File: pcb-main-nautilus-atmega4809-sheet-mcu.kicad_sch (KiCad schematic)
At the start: 20 parts, among them SW1 PTS645SH43SMTR92 LFS, U4 ATmega4809-A

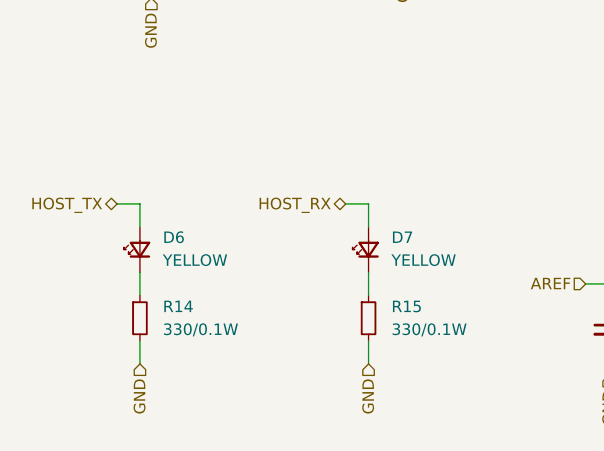
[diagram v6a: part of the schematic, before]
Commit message: Fix serial activity LEDs wiring
Supports #2.
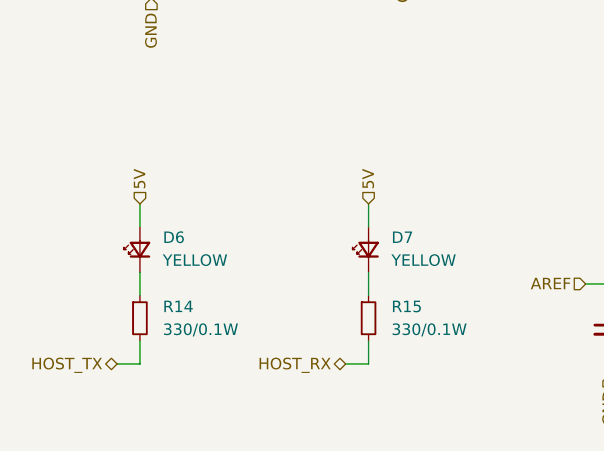
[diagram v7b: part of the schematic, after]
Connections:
- net 5V: now also D6.2 (A), D7.2 (A)
- net GND: no longer R14.2, R15.2
- net HOST_RX: now also R15.2; no longer D7.2 (A)
- net HOST_TX: now also R14.2; no longer D6.2 (A)
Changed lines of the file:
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@@
+    (stroke (width 0) (type default) (color 0 0 0 0))
+  )
+  (wire (pts (xy 44.45 127) (xy 44.45 129.54))
     (stroke (width 0) (type default) (color 0 0 0 0))
   )
@@
     (stroke (width 0) (type default) (color 0 0 0 0))
   )
+  (wire (pts (xy 142.24 54.61) (xy 142.24 64.77))
+    (stroke (width 0) (type default) (color 0 0 0 0))
+  )
+  (wire (pts (xy 147.32 64.77) (xy 142.24 64.77))
+    (stroke (width 0) (type default) (color 0 0 0 0))
+  )
+  (wire (pts (xy 67.31 144.78) (xy 69.85 144.78))
+    (stroke (width 0) (type default) (color 0 0 0 0))
+  )
+  (wire (pts (xy 154.94 102.87) (xy 157.48 102.87))
+    (stroke (width 0) (type default) (color 0 0 0 0))
+  )
+  (wire (pts (xy 73.66 96.52) (xy 73.66 99.06))
+    (stroke (width 0) (type default) (color 0 0 0 0))
+  )
+  (wire (pts (xy 154.94 133.35) (xy 157.48 133.35))
+    (stroke (width 0) (type default) (color 0 0 0 0))
+  )
+  (wire (pts (xy 71.12 88.9) (xy 73.66 88.9))
+    (stroke (width 0) (type default) (color 0 0 0 0))
+  )
+  (wire (pts (xy 198.12 78.74) (xy 200.66 78.74))
+    (stroke (width 0) (type default) (color 0 0 0 0))
+  )
+  (wire (pts (xy 121.92 87.63) (xy 124.46 87.63))
+    (stroke (width 0) (type default) (color 0 0 0 0))
+  )
+  (wire (pts (xy 73.66 88.9) (xy 73.66 91.44))
+    (stroke (width 0) (type default) (color 0 0 0 0))
+  )
+  (wire (pts (xy 198.12 76.2) (xy 200.66 76.2))
+    (stroke (width 0) (type default) (color 0 0 0 0))
+  )
+  (wire (pts (xy 111.76 135.89) (xy 111.76 138.43))
+    (stroke (width 0) (type default) (color 0 0 0 0))
+  )
+  (wire (pts (xy 121.92 92.71) (xy 124.46 92.71))
+    (stroke (width 0) (type default) (color 0 0 0 0))
+  )
+  (wire (pts (xy 205.74 76.2) (xy 208.28 76.2))
+    (stroke (width 0) (type default) (color 0 0 0 0))
+  )
+  (wire (pts (xy 205.74 88.9) (xy 208.28 88.9))
+    (stroke (width 0) (type default) (color 0 0 0 0))
+  )
+  (wire (pts (xy 147.32 54.61) (xy 142.24 54.61))
+    (stroke (width 0) (type default) (color 0 0 0 0))
+  )
+  (wire (pts (xy 154.94 128.27) (xy 157.48 128.27))
+    (stroke (width 0) (type default) (color 0 0 0 0))
+  )
+  (wire (pts (xy 154.94 100.33) (xy 157.48 100.33))
+    (stroke (width 0) (type default) (color 0 0 0 0))
+  )
+  (wire (pts (xy 198.12 88.9) (xy 200.66 88.9))
+    (stroke (width 0) (type default) (color 0 0 0 0))
+  )
+  (wire (pts (xy 124.46 44.45) (xy 124.46 54.61))
+    (stroke (width 0) (type default) (color 0 0 0 0))
+  )
+  (wire (pts (xy 45.72 101.6) (xy 45.72 104.14))
+    (stroke (width 0) (type default) (color 0 0 0 0))
+  )
+  (wire (pts (xy 139.7 64.77) (xy 139.7 72.39))
+    (stroke (width 0) (type default) (color 0 0 0 0))
+  )
+  (wire (pts (xy 121.92 107.95) (xy 124.46 107.95))
+    (stroke (width 0) (type default) (color 0 0 0 0))
+  )
+  (wire (pts (xy 96.52 138.43) (xy 96.52 135.89))
+    (stroke (width 0) (type default) (color 0 0 0 0))
+  )
+  (wire (pts (xy 124.46 54.61) (xy 124.46 64.77))
+    (stroke (width 0) (type default) (color 0 0 0 0))
+  )
+  (wire (pts (xy 129.54 44.45) (xy 124.46 44.45))
+    (stroke (width 0) (type default) (color 0 0 0 0))
+  )
   (wire (pts (xy 44.45 142.24) (xy 44.45 144.78))
     (stroke (width 0) (type default) (color 0 0 0 0))
   )
-  (wire (pts (xy 142.24 54.61) (xy 142.24 64.77))
-    (stroke (width 0) (type default) (color 0 0 0 0))
-  )
-  (wire (pts (xy 147.32 64.77) (xy 142.24 64.77))
-    (stroke (width 0) (type default) (color 0 0 0 0))
-  )
-  (wire (pts (xy 154.94 102.87) (xy 157.48 102.87))
-    (stroke (width 0) (type default) (color 0 0 0 0))
-  )
-  (wire (pts (xy 73.66 96.52) (xy 73.66 99.06))
-    (stroke (width 0) (type default) (color 0 0 0 0))
-  )
-  (wire (pts (xy 154.94 133.35) (xy 157.48 133.35))
-    (stroke (width 0) (type default) (color 0 0 0 0))
-  )
-  (wire (pts (xy 71.12 88.9) (xy 73.66 88.9))
-    (stroke (width 0) (type default) (color 0 0 0 0))
-  )
-  (wire (pts (xy 198.12 78.74) (xy 200.66 78.74))
-    (stroke (width 0) (type default) (color 0 0 0 0))
-  )
-  (wire (pts (xy 121.92 87.63) (xy 124.46 87.63))
-    (stroke (width 0) (type default) (color 0 0 0 0))
-  )
-  (wire (pts (xy 73.66 88.9) (xy 73.66 91.44))
-    (stroke (width 0) (type default) (color 0 0 0 0))
-  )
-  (wire (pts (xy 198.12 76.2) (xy 200.66 76.2))
-    (stroke (width 0) (type default) (color 0 0 0 0))
-  )
-  (wire (pts (xy 111.76 135.89) (xy 111.76 138.43))
-    (stroke (width 0) (type default) (color 0 0 0 0))
-  )
-  (wire (pts (xy 121.92 92.71) (xy 124.46 92.71))
-    (stroke (width 0) (type default) (color 0 0 0 0))
-  )
-  (wire (pts (xy 205.74 76.2) (xy 208.28 76.2))
-    (stroke (width 0) (type default) (color 0 0 0 0))
-  )
-  (wire (pts (xy 205.74 88.9) (xy 208.28 88.9))
-    (stroke (width 0) (type default) (color 0 0 0 0))
-  )
-  (wire (pts (xy 147.32 54.61) (xy 142.24 54.61))
-    (stroke (width 0) (type default) (color 0 0 0 0))
-  )
-  (wire (pts (xy 154.94 128.27) (xy 157.48 128.27))
-    (stroke (width 0) (type default) (color 0 0 0 0))
-  )
-  (wire (pts (xy 154.94 100.33) (xy 157.48 100.33))
-    (stroke (width 0) (type default) (color 0 0 0 0))
-  )
-  (wire (pts (xy 198.12 88.9) (xy 200.66 88.9))
-    (stroke (width 0) (type default) (color 0 0 0 0))
-  )
-  (wire (pts (xy 124.46 44.45) (xy 124.46 54.61))
-    (stroke (width 0) (type default) (color 0 0 0 0))
-  )
-  (wire (pts (xy 45.72 101.6) (xy 45.72 104.14))
-    (stroke (width 0) (type default) (color 0 0 0 0))
-  )
-  (wire (pts (xy 139.7 64.77) (xy 139.7 72.39))
-    (stroke (width 0) (type default) (color 0 0 0 0))
-  )
-  (wire (pts (xy 121.92 107.95) (xy 124.46 107.95))
-    (stroke (width 0) (type default) (color 0 0 0 0))
-  )
-  (wire (pts (xy 96.52 138.43) (xy 96.52 135.89))
-    (stroke (width 0) (type default) (color 0 0 0 0))
-  )
-  (wire (pts (xy 124.46 54.61) (xy 124.46 64.77))
-    (stroke (width 0) (type default) (color 0 0 0 0))
-  )
-  (wire (pts (xy 129.54 44.45) (xy 124.46 44.45))
-    (stroke (width 0) (type default) (color 0 0 0 0))
-  )
-  (wire (pts (xy 41.91 127) (xy 44.45 127))
-    (stroke (width 0) (type default) (color 0 0 0 0))
-  )
   (wire (pts (xy 121.92 105.41) (xy 124.46 105.41))
     (stroke (width 0) (type default) (color 0 0 0 0))
@@
     (stroke (width 0) (type default) (color 0 0 0 0))
   )
+  (wire (pts (xy 69.85 144.78) (xy 69.85 142.24))
+    (stroke (width 0) (type default) (color 0 0 0 0))
+  )
   (wire (pts (xy 69.85 134.62) (xy 69.85 137.16))
     (stroke (width 0) (type default) (color 0 0 0 0))
@@
     (stroke (width 0) (type default) (color 0 0 0 0))
   )
-  (wire (pts (xy 44.45 127) (xy 44.45 129.54))
-    (stroke (width 0) (type default) (color 0 0 0 0))
-  )
   (wire (pts (xy 124.46 54.61) (xy 129.54 54.61))
     (stroke (width 0) (type default) (color 0 0 0 0))
@@
     (stroke (width 0) (type default) (color 0 0 0 0))
   )
-  (wire (pts (xy 67.31 127) (xy 69.85 127))
-    (stroke (width 0) (type default) (color 0 0 0 0))
-  )
   (wire (pts (xy 154.94 130.81) (xy 157.48 130.81))
     (stroke (width 0) (type default) (color 0 0 0 0))
@@
     (stroke (width 0) (type default) (color 0 0 0 0))
   )
-  (wire (pts (xy 69.85 142.24) (xy 69.85 144.78))
-    (stroke (width 0) (type default) (color 0 0 0 0))
-  )
   (wire (pts (xy 96.52 143.51) (xy 96.52 146.05))
     (stroke (width 0) (type default) (color 0 0 0 0))
   )
+  (wire (pts (xy 44.45 144.78) (xy 41.91 144.78))
+    (stroke (width 0) (type default) (color 0 0 0 0))
+  )
   (wire (pts (xy 154.94 82.55) (xy 157.48 82.55))
     (stroke (width 0) (type default) (color 0 0 0 0))
@@
     (stroke (width 0) (type default) (color 0 0 0 0))
   )
+  (wire (pts (xy 69.85 127) (xy 69.85 129.54))
+    (stroke (width 0) (type default) (color 0 0 0 0))
+  )
   (wire (pts (xy 157.48 54.61) (xy 157.48 64.77))
     (stroke (width 0) (type default) (color 0 0 0 0))
@@
   )
   (wire (pts (xy 139.7 143.51) (xy 139.7 146.05))
-    (stroke (width 0) (type default) (color 0 0 0 0))
-  )
-  (wire (pts (xy 69.85 127) (xy 69.85 129.54))
     (stroke (width 0) (type default) (color 0 0 0 0))
   )
@@
     (effects (font (size 1.27 1.27)) (justify left))
   )
-  (hierarchical_label "HOST_TX" (shape bidirectional) (at 41.91 127 180)
-    (effects (font (size 1.27 1.27)) (justify right))
-  )
-  (hierarchical_label "GND" (shape input) (at 44.45 144.78 270)
+  (hierarchical_label "HOST_TX" (shape bidirectional) (at 41.91 144.78 180)
     (effects (font (size 1.27 1.27)) (justify right))
   )
@@
     (effects (font (size 1.27 1.27)) (justify right))
   )
-  (hierarchical_label "HOST_RX" (shape bidirectional) (at 67.31 127 180)
+  (hierarchical_label "HOST_RX" (shape bidirectional) (at 67.31 144.78 180)
     (effects (font (size 1.27 1.27)) (justify right))
   )
@@
     (effects (font (size 1.27 1.27)) (justify right))
   )
+  (hierarchical_label "5V" (shape input) (at 69.85 127 90)
+    (effects (font (size 1.27 1.27)) (justify left))
+  )
   (hierarchical_label "UPDI" (shape bidirectional) (at 121.92 77.47 180)
     (effects (font (size 1.27 1.27)) (justify right))
@@
     (effects (font (size 1.27 1.27)) (justify right))
   )
-  (hierarchical_label "GND" (shape input) (at 69.85 144.78 270)
-    (effects (font (size 1.27 1.27)) (justify right))
-  )
   (hierarchical_label "~{RESET}" (shape bidirectional) (at 76.2 88.9 0)
     (effects (font (size 1.27 1.27)) (justify left))
@@
     (effects (font (size 1.27 1.27)) (justify right))
   )
+  (hierarchical_label "5V" (shape input) (at 44.45 127 90)
+    (effects (font (size 1.27 1.27)) (justify left))
+  )
   (symbol (lib_id "Device:R_Small") (at 203.2 114.3 0) (unit 1)

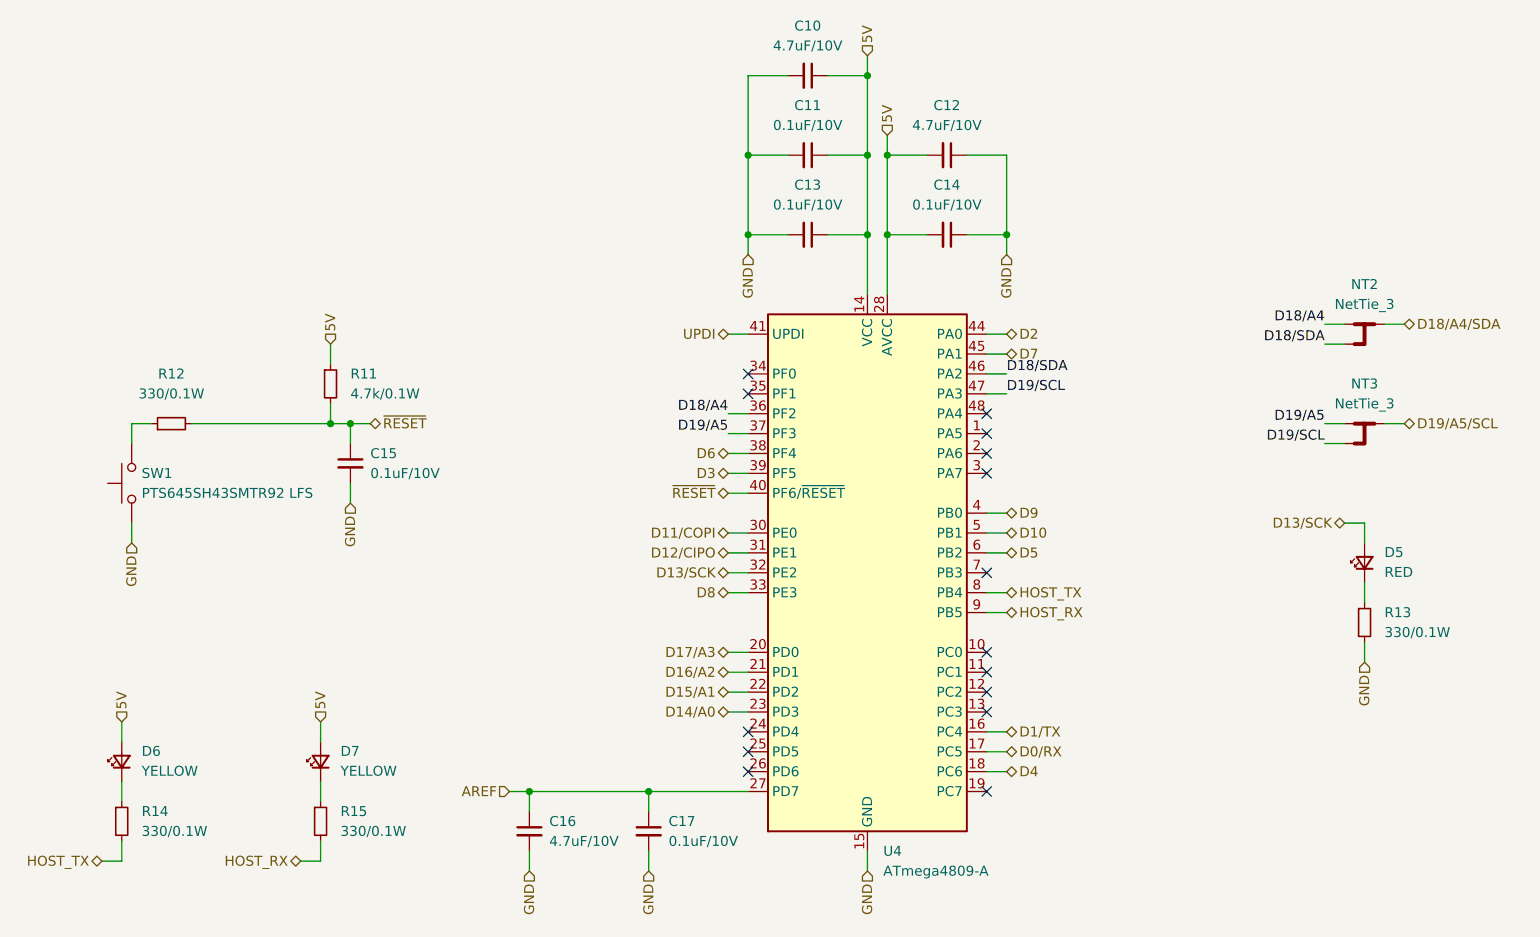
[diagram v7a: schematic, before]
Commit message: Improve MCU sheet flow
Supports #2.
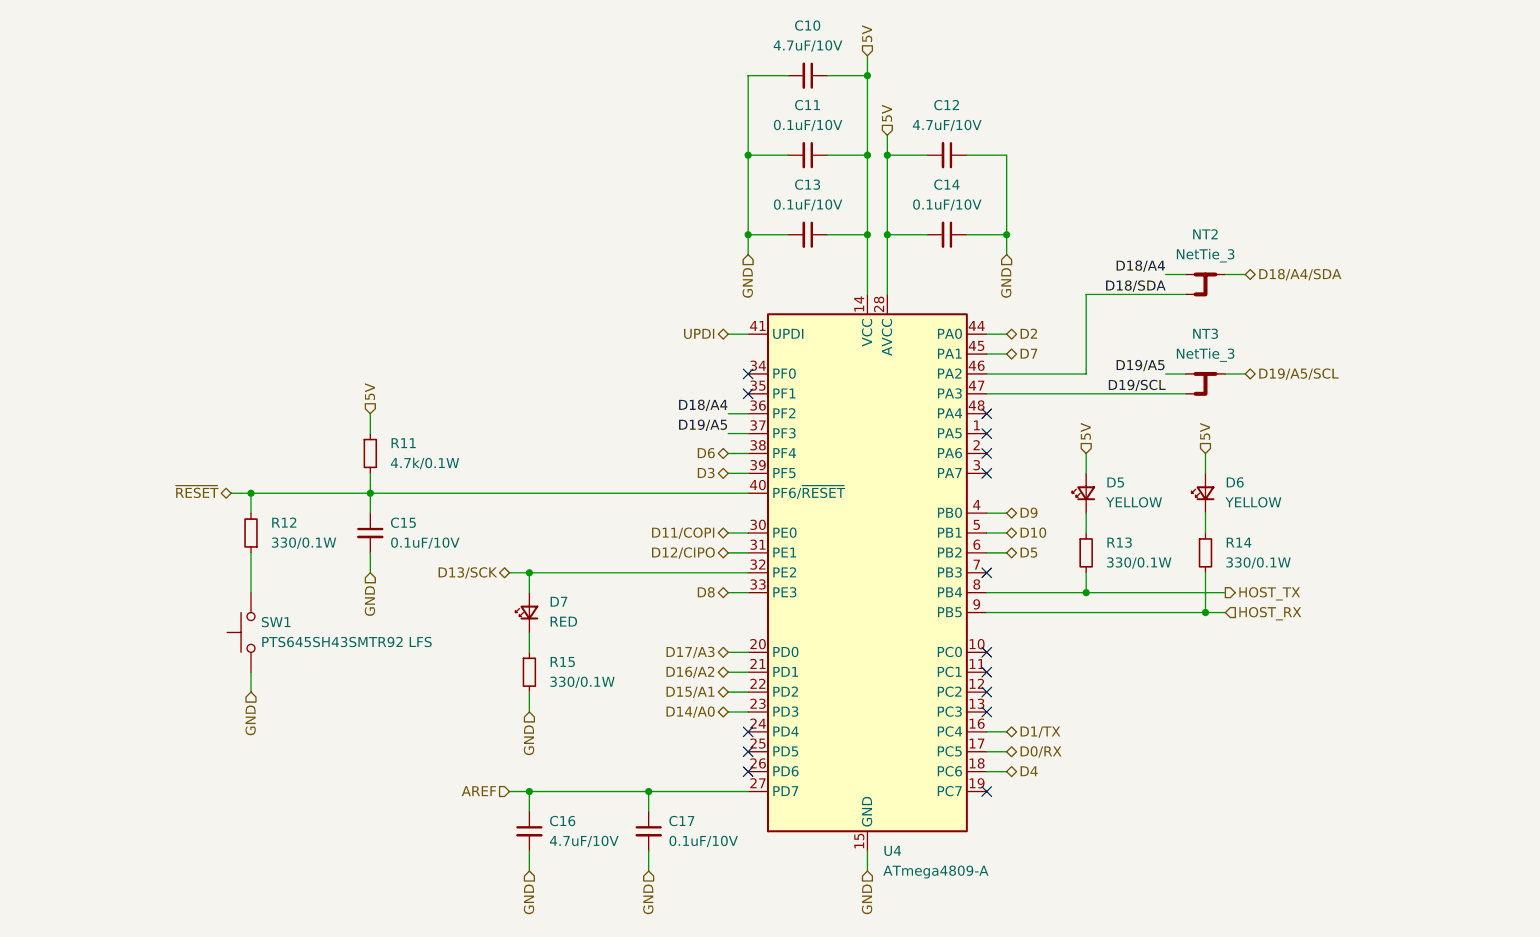
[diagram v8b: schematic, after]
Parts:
- renumbered D6 to D5, D7 to D6, D5 to D7, R14 to R13, R15 to R14, R13 to R15
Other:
- moved on the sheet: C15, D5, D6, D7, NT2, NT3, R11, R12, R13, R14, R15, SW1
